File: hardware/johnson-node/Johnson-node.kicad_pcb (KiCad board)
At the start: 2 copper layers, 78 x 58 mm, 13 parts, among them J1 Conn_01x02, J10 Conn_01x03, J11 Conn_01x03, J12 Conn_01x12, J2 Conn_01x03, J3 Conn_01x03, J4 Conn_01x03, J5 Conn_01x03, J6 Conn_01x03, J7 Conn_01x03, J8 Conn_01x03, J9 Conn_01x03

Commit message: hats
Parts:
- added C1: 1u, Capacitor_SMD:C_0603_1608Metric, F.Cu at (196.5, 65.3)
- added C10: 4.7u, Capacitor_SMD:C_0603_1608Metric, F.Cu at (200.5, 70.3)
- added C11: 0.1u, Capacitor_SMD:C_0603_1608Metric, F.Cu at (200.5, 72.8)
- added C12: 0.1u, Capacitor_SMD:C_0603_1608Metric, F.Cu at (200.5, 75.3)
- added C13: 1u, Capacitor_SMD:C_0603_1608Metric, F.Cu at (200.5, 77.8)
- added C15: 2.2u, Capacitor_SMD:C_0603_1608Metric, F.Cu at (200.5, 80.3)
- added C16: 100n, Capacitor_SMD:C_0603_1608Metric, F.Cu at (204.5, 65.3)
- added C17: 100n, Capacitor_SMD:C_0603_1608Metric, F.Cu at (204.5, 67.8)
- added C18: 10u, Capacitor_SMD:C_0603_1608Metric, F.Cu at (204.5, 70.3)
- added C19: 1u, Capacitor_SMD:C_0603_1608Metric, F.Cu at (204.5, 72.8)
- added C2: 10u, Capacitor_SMD:C_0603_1608Metric, F.Cu at (196.5, 67.8)
- added C20: 1u, Capacitor_SMD:C_0603_1608Metric, F.Cu at (204.5, 75.3)
- added C21: 0.1u, Capacitor_SMD:C_0603_1608Metric, F.Cu at (204.5, 77.8)
- added C22: 0.1u, Capacitor_SMD:C_0603_1608Metric, F.Cu at (204.5, 80.3)
- added C3: 0.1u, Capacitor_SMD:C_0603_1608Metric, F.Cu at (196.5, 70.3)
- added C4: 100n, Capacitor_SMD:C_0603_1608Metric, F.Cu at (196.5, 72.8)
- added C5: 10u, Capacitor_SMD:C_0603_1608Metric, F.Cu at (196.5, 75.3)
- added C6: 22u, Capacitor_SMD:C_0603_1608Metric, F.Cu at (196.5, 77.8)
- added C7: 0.1u, Capacitor_SMD:C_0603_1608Metric, F.Cu at (196.5, 80.3)
- added C8: 0.1u, Capacitor_SMD:C_0603_1608Metric, F.Cu at (200.5, 65.3)
- added C9: 100n, Capacitor_SMD:C_0603_1608Metric, F.Cu at (200.5, 67.8)
- added IC1: ADC124S051CIMM_NOPB, CustomFootprints:SOP50P490X110-10N, F.Cu at (185.5, 87.6)
- added IC2: ADC124S051CIMM_NOPB, CustomFootprints:SOP50P490X110-10N, F.Cu at (185.5, 92.2)
- added J13: BSEL, Connector_PinHeader_2.54mm:PinHeader_1x02_P2.54mm_Vertical, F.Cu at (196.8, 91.0)
- added J14: RST, Connector_PinHeader_2.54mm:PinHeader_1x02_P2.54mm_Vertical, F.Cu at (201.4, 91.0)
- added L1: 2.2u, Inductor_SMD:L_0603_1608Metric, F.Cu at (208.5, 65.3)
- added L2: 5.6u, Inductor_SMD:L_0603_1608Metric, F.Cu at (208.5, 67.8)
- added R1: 27, Resistor_SMD:R_0603_1608Metric, F.Cu at (208.5, 70.3)
- added R2: 27, Resistor_SMD:R_0603_1608Metric, F.Cu at (208.5, 72.8)
- added R3: 10k, Resistor_SMD:R_0603_1608Metric, F.Cu at (208.5, 75.3)
- added R7: 0, Resistor_SMD:R_0603_1608Metric, F.Cu at (208.5, 77.8)
- added U1: ESP32-S3-WROOM-1U-N4R2, CustomFootprints:XCVR_ESP32-S3-WROOM-1U-N4R2, F.Cu at (113.3, 65.1)
- added U2: LMR50410Y3FQDBVRQ1, CustomFootprints:SOT95P280X145-6N, F.Cu at (191.8, 87.5)
- added U3: LMR50410Y5FQDBVRQ1, Custom_MSM:Regulator_Switching_SOT-23-6, F.Cu at (176.5, 94.2)
- added U4: ISO1042BQDWVQ1, CustomFootprints:DWV0008A-MFG, F.Cu at (186.8, 107.2)
- added U5: MAX3390EEUD_T, CustomFootprints:SOP65P640X110-14N, F.Cu at (177.4, 88.6)
- moved J12 0.50 mm to (148.0, 80.5)
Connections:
- J1 pad 1: unconnected-(J1-Pin_1-Pad1) -> GND
- J1 pad 2: unconnected-(J1-Pin_2-Pad2) -> BATT
- J10 pad 1: unconnected-(J10-Pin_1-Pad1) -> GND
- J10 pad 3: unconnected-(J10-Pin_3-Pad3) -> +5V
- J11 pad 1: unconnected-(J11-Pin_1-Pad1) -> GND
- J11 pad 3: unconnected-(J11-Pin_3-Pad3) -> +5V
- J2 pad 1: unconnected-(J2-Pin_1-Pad1) -> GND
- J2 pad 3: unconnected-(J2-Pin_3-Pad3) -> +5V
- J3 pad 1: unconnected-(J3-Pin_1-Pad1) -> GND
- J3 pad 3: unconnected-(J3-Pin_3-Pad3) -> +5V
- J4 pad 1: unconnected-(J4-Pin_1-Pad1) -> GND
- J4 pad 3: unconnected-(J4-Pin_3-Pad3) -> +5V
- J5 pad 1: unconnected-(J5-Pin_1-Pad1) -> GND
- J5 pad 3: unconnected-(J5-Pin_3-Pad3) -> +5V
- J6 pad 1: unconnected-(J6-Pin_1-Pad1) -> GND
- J6 pad 3: unconnected-(J6-Pin_3-Pad3) -> +5V
- J7 pad 1: unconnected-(J7-Pin_1-Pad1) -> GND
- J7 pad 3: unconnected-(J7-Pin_3-Pad3) -> +5V
- J8 pad 1: unconnected-(J8-Pin_1-Pad1) -> GND
- J8 pad 3: unconnected-(J8-Pin_3-Pad3) -> +5V
- J9 pad 1: unconnected-(J9-Pin_1-Pad1) -> GND
- J9 pad 3: unconnected-(J9-Pin_3-Pad3) -> +5V

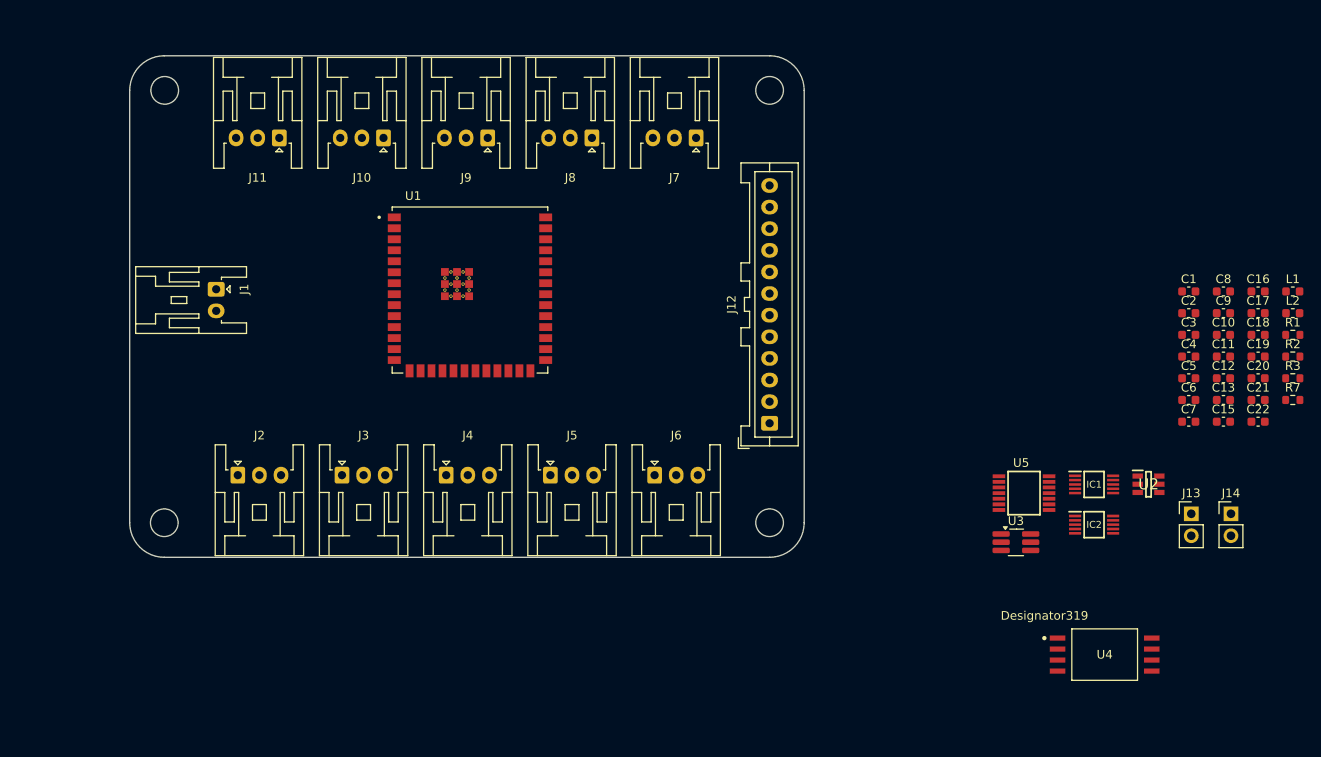
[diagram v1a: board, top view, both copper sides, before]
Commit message: placement of components
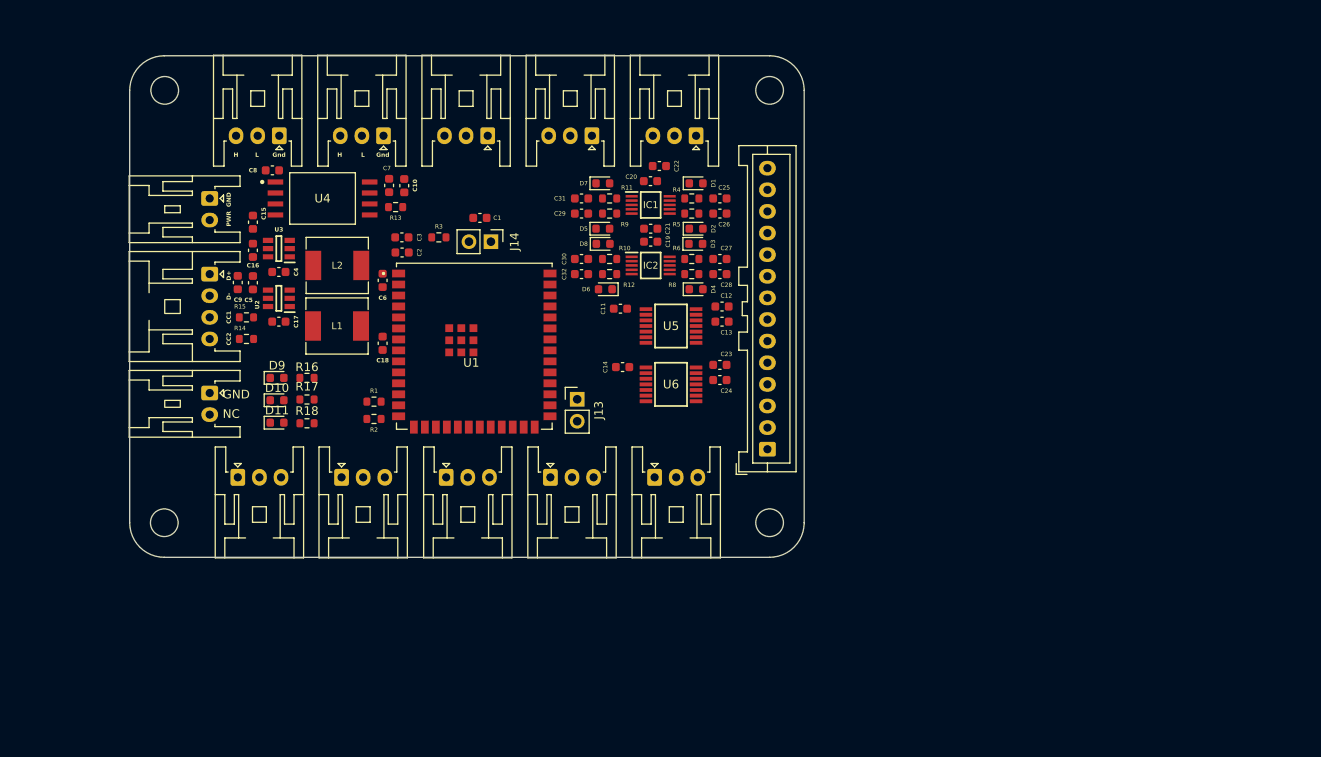
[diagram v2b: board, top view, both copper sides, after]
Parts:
- removed J12: Conn_01x12, Connector_JST:JST_XA_B12B-XASK-1_1x12_P2.50mm_Vertical
- removed R7: 0, Resistor_SMD:R_0603_1608Metric
- added C14: 0.1u, Capacitor_SMD:C_0603_1608Metric, F.Cu at (131.0, 74.0)
- added C23: 0.1u, Capacitor_SMD:C_0603_1608Metric, F.Cu at (142.2, 73.8)
- added C24: 1u, Capacitor_SMD:C_0603_1608Metric, F.Cu at (142.2, 75.5)
- added C25: 33n, Capacitor_SMD:C_0603_1608Metric, F.Cu at (142.2, 54.5)
- added C26: 33n, Capacitor_SMD:C_0603_1608Metric, F.Cu at (142.2, 56.2)
- added C27: 33n, Capacitor_SMD:C_0603_1608Metric, F.Cu at (142.2, 61.5)
- added C28: 33n, Capacitor_SMD:C_0603_1608Metric, F.Cu at (142.2, 63.2)
- added C29: 33n, Capacitor_SMD:C_0603_1608Metric, F.Cu at (126.2, 56.2)
- added C30: 33n, Capacitor_SMD:C_0603_1608Metric, F.Cu at (126.2, 61.5)
- added C31: 33n, Capacitor_SMD:C_0603_1608Metric, F.Cu at (126.2, 54.5)
- added C32: 33n, Capacitor_SMD:C_0603_1608Metric, F.Cu at (126.2, 63.2)
- added D1: D_Schottky, Diode_SMD:D_0603_1608Metric, F.Cu at (139.5, 52.8)
- added D10: RED LED, LED_SMD:LED_0603_1608Metric, F.Cu at (91.0, 77.8)
- added D11: RED LED, LED_SMD:LED_0603_1608Metric, F.Cu at (91.0, 80.4)
- added D2: D_Schottky, Diode_SMD:D_0603_1608Metric, F.Cu at (139.5, 58.0)
- added D3: D_Schottky, Diode_SMD:D_0603_1608Metric, F.Cu at (139.5, 59.8)
- added D4: D_Schottky, Diode_SMD:D_0603_1608Metric, F.Cu at (139.5, 65.0)
- added D5: D_Schottky, Diode_SMD:D_0603_1608Metric, F.Cu at (128.7, 58.0)
- added D6: D_Schottky, Diode_SMD:D_0603_1608Metric, F.Cu at (129.0, 65.0)
- added D7: D_Schottky, Diode_SMD:D_0603_1608Metric, F.Cu at (128.7, 52.8)
- added D8: D_Schottky, Diode_SMD:D_0603_1608Metric, F.Cu at (128.8, 59.8)
- added D9: RED LED, LED_SMD:LED_0603_1608Metric, F.Cu at (91.0, 75.2)
- added J15: SO4B-XASK-1, Connector_JST:JST_XA_S04B-XASK-1_1x04_P2.50mm_Horizontal, F.Cu at (83.2, 63.2)
- added J16: Conn_01x02, Connector_JST:JST_XA_S02B-XASK-1_1x02_P2.50mm_Horizontal, F.Cu at (83.2, 77.0)
- added J17: Conn_01x14, Connector_JST:JST_XA_B14B-XASK-1_1x14_P2.50mm_Vertical, F.Cu at (147.8, 83.5)
- added R10: 100R, Resistor_SMD:R_0603_1608Metric, F.Cu at (129.5, 61.5)
- added R11: 100R, Resistor_SMD:R_0603_1608Metric, F.Cu at (129.5, 54.5)
- added R12: 100R, Resistor_SMD:R_0603_1608Metric, F.Cu at (129.5, 63.2)
- added R13: 120, Resistor_SMD:R_0603_1608Metric, F.Cu at (104.8, 55.5)
- added R14: 5k1, Resistor_SMD:R_0603_1608Metric, F.Cu at (87.5, 70.8)
- added R15: 5k1, Resistor_SMD:R_0603_1608Metric, F.Cu at (87.5, 68.2)
- added R16: 270R, Resistor_SMD:R_0603_1608Metric, F.Cu at (94.5, 75.2)
- added R17: 620R, Resistor_SMD:R_0603_1608Metric, F.Cu at (94.5, 77.8)
- added R18: 270R, Resistor_SMD:R_0603_1608Metric, F.Cu at (94.5, 80.5)
- added R4: 100R, Resistor_SMD:R_0603_1608Metric, F.Cu at (139.0, 54.5)
- added R5: 100R, Resistor_SMD:R_0603_1608Metric, F.Cu at (139.0, 56.2)
- added R6: 100R, Resistor_SMD:R_0603_1608Metric, F.Cu at (139.0, 61.5)
- added R8: 100R, Resistor_SMD:R_0603_1608Metric, F.Cu at (139.0, 63.2)
- added R9: 100R, Resistor_SMD:R_0603_1608Metric, F.Cu at (129.5, 56.2)
- added U6: MAX3390EEUD_T, CustomFootprints:SOP65P640X110-14N, F.Cu at (136.6, 76.0)
- C15: value 2.2u -> 10u
- C6: value 22u -> 10u
- L1, L2: footprint Inductor_SMD:L_0603_1608Metric -> CustomFootprints:Shielded_Inductor_SMD_7265
- U3: footprint Custom_MSM:Regulator_Switching_SOT-23-6 -> CustomFootprints:SOT95P280X145-6N
- moved C16 116.3 mm to (88.2, 60.5), turned to -90 degrees
- moved C15 114.6 mm to (88.2, 57.2), turned to 90 degrees
- moved C9 114.0 mm to (86.5, 64.2), turned to 90 degrees
- moved C17 113.2 mm to (91.2, 68.8)
- moved C8 110.9 mm to (90.5, 51.2), turned to 180 degrees
- moved L2 110.6 mm to (98.0, 62.2)
- moved L1 110.6 mm to (98.0, 69.2)
- moved C5 108.8 mm to (88.2, 64.2), turned to 90 degrees
- moved R1 106.5 mm to (102.2, 78.0), turned to 180 degrees
- moved R2 106.5 mm to (102.2, 80.0), turned to 180 degrees
- moved C4 105.7 mm to (91.2, 63.0)
- moved U4 104.7 mm to (96.3, 54.5)
- moved U2 102.8 mm to (91.2, 66.0), turned to 180 degrees
- moved C18 101.2 mm to (103.2, 71.2), turned to -90 degrees
- moved R3 100.1 mm to (109.8, 59.0)
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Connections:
- net CS renamed CS_A
- C19 pad 1: +5V_Supply -> +5V
- C20 pad 1: +5V_Supply -> +5V
- C21 pad 1: +5V_Supply -> +5V
- C22 pad 1: +5V_Supply -> +5V
- IC1 pad 1: CS1 -> 5V_CS_A
- IC1 pad 10: Net-(IC1-SCLK) -> 5V_SCLK
- IC1 pad 2: +5V_Supply -> +5V
- IC1 pad 4: SGDOUT -> SGD_P
- IC1 pad 5: SGCOUT -> SGC_P
- IC1 pad 6: SGBOUT -> SGB_P
- IC1 pad 7: SGAOUT -> SGA_P
- IC1 pad 8: DIN -> 5V_MOSI
- IC1 pad 9: Net-(IC1-DOUT) -> 5V_MISO
- IC2 pad 1: CS2 -> 5V_CS_B
- IC2 pad 10: Net-(IC1-SCLK) -> 5V_SCLK
- IC2 pad 2: +5V_Supply -> +5V
- IC2 pad 4: SGHOUT -> SGH_P
- IC2 pad 5: SGGOUT -> SGG_P
- IC2 pad 6: SGFOUT -> SGF_P
- IC2 pad 7: SGEOUT -> SGE_P
- IC2 pad 8: DIN -> 5V_MOSI
- IC2 pad 9: Net-(IC1-DOUT) -> 5V_MISO
- J10 pad 2: unconnected-(J10-Pin_2-Pad2) -> CANL
- J10 pad 3: +5V -> CANH
- J11 pad 2: unconnected-(J11-Pin_2-Pad2) -> CANL
- J11 pad 3: +5V -> CANH
- J2 pad 2: unconnected-(J2-Pin_2-Pad2) -> SGA
- J3 pad 2: unconnected-(J3-Pin_2-Pad2) -> SGC
- J4 pad 2: unconnected-(J4-Pin_2-Pad2) -> SGB
- J5 pad 2: unconnected-(J5-Pin_2-Pad2) -> SGD
- J6 pad 2: unconnected-(J6-Pin_2-Pad2) -> SGE
- J7 pad 2: unconnected-(J7-Pin_2-Pad2) -> SGF
- J8 pad 2: unconnected-(J8-Pin_2-Pad2) -> SGG
- J9 pad 2: unconnected-(J9-Pin_2-Pad2) -> SGH
- U1 pad 12: FLATSHIFT -> CS_C
- U1 pad 17: PWM -> CS_B
- U1 pad 24: UP -> unconnected-(U1-IO47-Pad24)
- U1 pad 25: DOWN -> unconnected-(U1-IO48-Pad25)
- U1 pad 26: NEUTRAL -> unconnected-(U1-IO45-Pad26)
- U1 pad 28: unconnected-(U1-IO35-Pad28) -> Net-(U1-IO35)
- U1 pad 5: NEUTRAL_LED -> unconnected-(U1-IO5-Pad5)
- U1 pad 6: DOWN_LED -> unconnected-(U1-IO6-Pad6)
- U1 pad 7: UP_LED -> CS_D
- U3 pad 4: Net-(U3-EN) -> BATT
- U5 pad 10: E_CS -> 5V_CS_A
- U5 pad 11: E_SCLK -> 5V_SCLK
- U5 pad 12: E_MOSI -> 5V_MOSI
- U5 pad 13: E_MISO -> 5V_MISO
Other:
- board text added: "CC1"
- board text added: "CC2"
- board text added: "D+"
- board text added: "D-"
- board text added: "GND"
- board text added: "Gnd"
- board text added: "H"
- board text added: "L"
- board text added: "NC"
- board text added: "PWR"

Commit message: minor changes
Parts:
- added G***: LOGO, LOGO, F.Cu at (135.8, 79.8)
- added G***: LOGO, LOGO, B.Cu at (101.9, 72.6)
- added REF**: jamesp-F.Cu, CustomFootprints:jamesp-F.Cu, F.Cu at (110.8, 53.0)
- moved STATUS 3.82 mm to (94.2, 78.2)
- moved R18 3.72 mm to (97.5, 78.2), turned to 180 degrees
- moved +5V 3.41 mm to (94.2, 76.5)
- moved R17 3.22 mm to (97.5, 76.5)
- moved +3V3 3.21 mm to (94.2, 74.8)
- moved R16 3.00 mm to (97.5, 74.8)
- moved C11 2.60 mm to (132.8, 65.7)
- moved C32 1.75 mm to (126.3, 61.5)
- moved C30 1.75 mm to (126.3, 63.2)
- moved R10 1.75 mm to (129.5, 63.2)
- moved R12 1.75 mm to (129.5, 61.5)
- moved C14 1.10 mm to (131.0, 72.9)
- moved C17 1.01 mm to (91.4, 69.8), turned to 180 degrees
- moved U2 0.60 mm to (91.2, 66.7), turned to -90 degrees
- moved R13 0.40 mm to (104.8, 55.9)
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- renumbered D9 to +3V3, D10 to +5V, D11 to STATUS
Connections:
- J17 pad 11: +12V -> BATT
- J17 pad 13: +12V -> BATT
- R18 pad 1: Net-(U1-IO35) -> Net-(U1-IO18)
- U1 pad 11: unconnected-(U1-IO18-Pad11) -> Net-(U1-IO18)
- U1 pad 28: Net-(U1-IO35) -> unconnected-(U1-IO35-Pad28)
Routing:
- net +5V: track 0.00 -> 326.3 mm, vias 0 -> 7
- net +3V3: track 0.00 -> 161.8 mm
- net BATT: track 0.00 -> 126.3 mm
- net SGA: track 0.00 -> 81.4 mm, vias 0 -> 1
- net SGB: track 0.00 -> 63.2 mm, vias 0 -> 1
- net SGC: track 0.00 -> 56.0 mm, vias 0 -> 1
- net SGE: track 0.00 -> 50.2 mm, vias 0 -> 1
- net CANH: track 0.00 -> 43.3 mm
- net 5V_SCLK: track 0.00 -> 41.5 mm, vias 0 -> 3
- net CANR: track 0.00 -> 41.5 mm
- net CAND: track 0.00 -> 41.4 mm
- net 5V_MOSI: track 0.00 -> 40.3 mm, vias 0 -> 3
- net USBD+: track 0.00 -> 39.1 mm
- net USBD-: track 0.00 -> 37.3 mm
- net SGD: track 0.00 -> 35.6 mm, vias 0 -> 1
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- added copper zone on B.Cu, net GND
- added copper zone on F.Cu, net GND
- added copper zone on F.Cu, net Net-(U2-SW)
- added copper zone on F.Cu, net Net-(U3-SW)
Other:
- board text added: "BOOT"
- board text added: "Johnson Node V3.0 Designed by James Platt Routed 13/05/26"
- board text added: "RST"

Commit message: add onboard reg
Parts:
- moved REF** 45.6 mm to (78.8, 85.5)
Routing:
- net GND: vias 26 -> 29
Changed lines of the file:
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@@
 	(footprint "CustomFootprints:jamesp-F.Cu"
 		(layer "F.Cu")
-		(at 110.75 53)
+		(at 78.75 85.5)
 		(property "Reference" "REF**"
 			(at 6.131634 -0.258666 0)
@@
 	)
 	(via
+		(at 122.6 63.18)
+		(size 0.6)
+		(drill 0.3)
+		(layers "F.Cu" "B.Cu")
+		(net "GND")
+	)
+	(via
 		(at 100.15 65.2)
 		(size 0.6)
@@
 	)
 	(via
+		(at 110.75 52.25)
+		(size 0.6)
+		(drill 0.3)
+		(layers "F.Cu" "B.Cu")
+		(free yes)
+		(net "GND")
+	)
+	(via
 		(at 102.9 59.2)
 		(size 0.6)
@@
 		(net "GND")
 	)
+	(via
+		(at 105.1 63.18)
+		(size 0.6)
+		(drill 0.3)
+		(layers "F.Cu" "B.Cu")
+		(net "GND")
+	)

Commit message: grounding
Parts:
- renumbered +5V to D10, STATUS to D11, +3V3 to D9
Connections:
- J17 pad 10: unconnected-(J17-Pin_10-Pad10) -> TX
- J17 pad 6: unconnected-(J17-Pin_6-Pad6) -> PPS
- J17 pad 7: unconnected-(J17-Pin_7-Pad7) -> SCL
- J17 pad 8: unconnected-(J17-Pin_8-Pad8) -> SDA
- J17 pad 9: unconnected-(J17-Pin_9-Pad9) -> RX
- U1 pad 10: unconnected-(U1-IO17-Pad10) -> PPS
- U1 pad 36: RX -> unconnected-(U1-RXD0-Pad36)
- U1 pad 37: TX -> unconnected-(U1-TXD0-Pad37)
- U1 pad 5: unconnected-(U1-IO5-Pad5) -> RX
- U1 pad 6: unconnected-(U1-IO6-Pad6) -> TX
- U1 pad 8: unconnected-(U1-IO15-Pad8) -> SDA
- U1 pad 9: unconnected-(U1-IO16-Pad9) -> SCL
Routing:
- net SCL: track 0.00 -> 80.2 mm, vias 0 -> 2
- net SDA: track 0.00 -> 77.7 mm, vias 0 -> 2
- net RX: track 0.00 -> 74.3 mm, vias 0 -> 2
- net PPS: track 0.00 -> 74.0 mm, vias 0 -> 2
- net TX: track 0.00 -> 73.9 mm, vias 0 -> 2
- net GND: track 21.4 -> 27.3 mm, vias 29 -> 36
- net SGH: track 24.9 -> 26.3 mm

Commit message: 3d models
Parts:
- L1, L2: footprint CustomFootprints:Shielded_Inductor_SMD_7265 -> CustomFootprints:WE-TPC_4828
- moved L2 0.79 mm to (97.2, 62.2), turned to 90 degrees
- moved L1 0.75 mm to (97.2, 69.0), turned to 90 degrees
- renumbered D9 to +3V3, D10 to +5V, D11 to STATUS
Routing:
- net +5V: track 326.3 -> 328.9 mm
- net Net-(U3-CB): track 17.5 -> 19.3 mm
